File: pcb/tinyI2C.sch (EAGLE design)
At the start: 29 parts, among them IC1 74ABT125BQ, IC2 TPS73618(0.4A), U1 LPC824M201JHI33, X1 TSW-112-02-S-S, X2 TSW-106-02-S-S-RA, X3 TSW-112-02-S-S, X4 TSW-102-02-S-S, X5 TSW-102-02-S-S

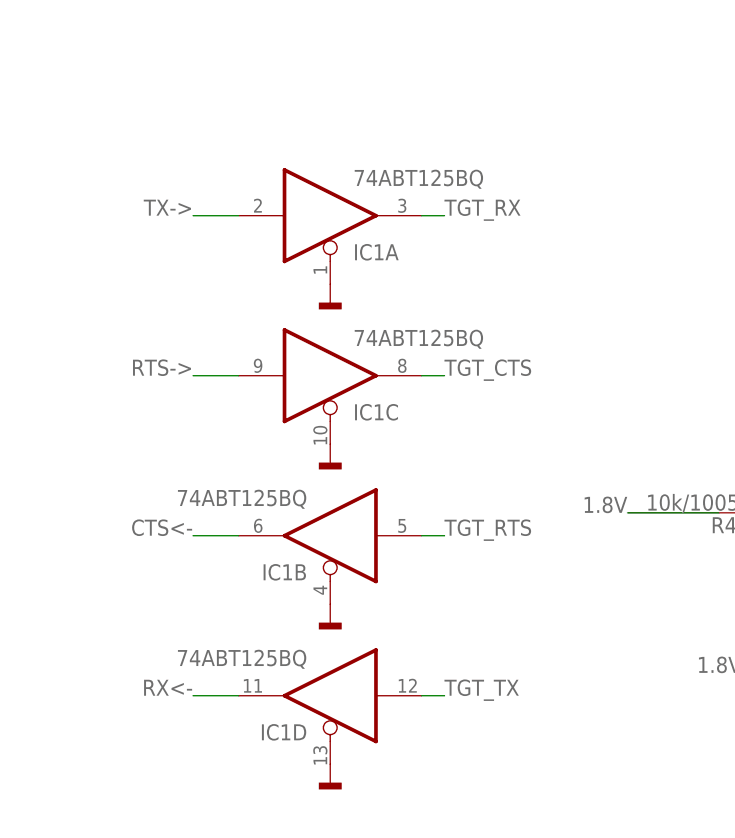
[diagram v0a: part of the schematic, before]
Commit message: [ PCB ][ SCH ][ BRD ] IC1, C5 update IC1: better footprint C5: smaller footprint
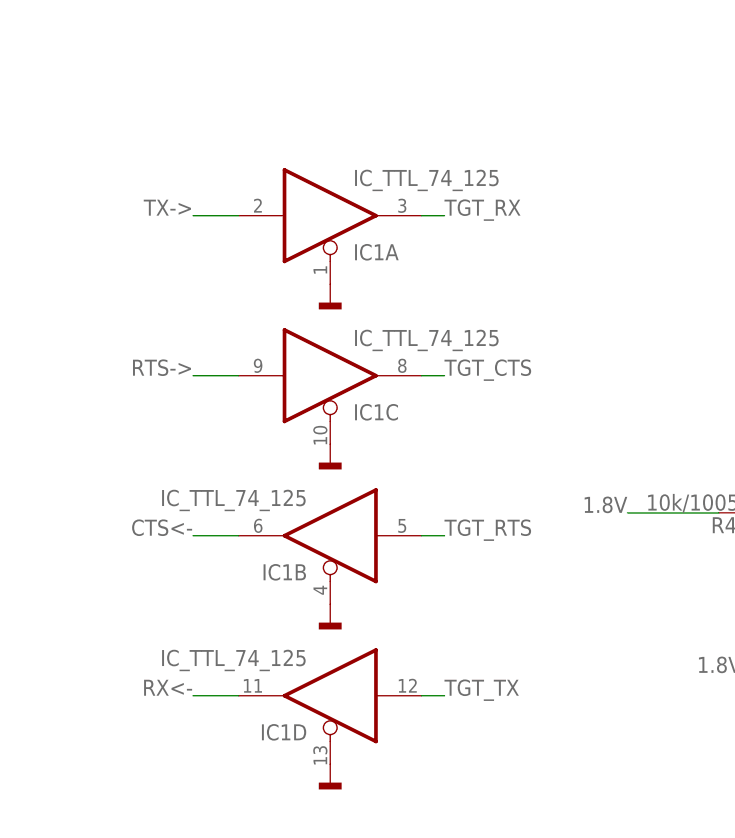
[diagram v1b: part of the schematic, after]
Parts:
- C5: device rcl:C-EUC1608 -> rcl:C-EUC0402
- IC1: value 74ABT125BQ -> IC_TTL_74_125; device 74xx-eu_local:74ABT125BQ -> mylib:IC_TTL_74_125
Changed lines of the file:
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@@
 <part name="C2" library="rcl" deviceset="C-EU" device="C1005" value="1005"/>
 <part name="C4" library="rcl" deviceset="C-EU" device="C1005" value="1005"/>
-<part name="C5" library="rcl" deviceset="C-EU" device="C1608" value="1608"/>
+<part name="C5" library="rcl" deviceset="C-EU" device="C0402" value="1608"/>
 <part name="GND9" library="mbed-HDK" deviceset="GND" device=""/>
 <part name="GND10" library="mbed-HDK" deviceset="GND" device=""/>
@@
 <part name="GND13" library="mbed-HDK" deviceset="GND" device=""/>
 <part name="C6" library="rcl" deviceset="C-EU" device="C1005" value="1005"/>
-<part name="IC1" library="74xx-eu_local" deviceset="74*125" device="BQ" technology="ABT"/>
+<part name="IC1" library="mylib" deviceset="IC_TTL_74_125" device=""/>
 <part name="X4" library="con-samtec.local" deviceset="TSW-102-02-S-S" device=""/>
 <part name="GND12" library="mbed-HDK" deviceset="GND" device=""/>

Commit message: [ PCB ][ SCH ] new header for ISP
added ISP header
removed connection to X1[3]
renamed other headers
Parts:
- added X6: TSW-102-02-S-S, con-samtec.local:TSW-102-02-S-S
- X2: value TSW-106-02-S-S-RA -> TSW-112-02-S-S; device con-samtec.local:TSW-106-02-S-S-RA -> con-samtec.local:TSW-112-02-S-S
- X3: value TSW-112-02-S-S -> TSW-106-02-S-S-RA; device con-samtec.local:TSW-112-02-S-S -> con-samtec.local:TSW-106-02-S-S-RA
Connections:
- net !ISP!: now also X6-1.1; no longer X1-3.1
- net 5V: now also X3-3.1; no longer X2-3.1
- net CTS<-: now also X3-2.1; no longer X2-2.1
- net GND: now also X3-1.1, X6-2.1; no longer X2-1.1
- net GPIO00: now also X2-1.1; no longer X3-1.1
- net GPIO01: now also X2-2.1; no longer X3-2.1
- net GPIO02: now also X2-3.1; no longer X3-3.1
- net GPIO03: now also X2-4.1; no longer X3-4.1
- net GPIO04: now also X2-5.1; no longer X3-5.1
- net GPIO05: now also X2-6.1; no longer X3-6.1
- net GPIO06: now also X2-7.1; no longer X3-7.1
- net GPIO07: now also X2-8.1; no longer X3-8.1
- net RTS->: now also X3-6.1; no longer X2-6.1
- net RX<-: now also X3-5.1; no longer X2-5.1
- net SPI_CS: now also X2-12.1; no longer X3-12.1
- net SPI_MISO: now also X2-10.1; no longer X3-10.1
- net SPI_MOSI: now also X2-9.1; no longer X3-9.1
- net SPI_SCK: now also X2-11.1; no longer X3-11.1
- net TX->: now also X3-4.1; no longer X2-4.1
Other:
- moved on the sheet: X2-1, X2-2, X2-3, X2-4, X2-5, X2-6, X3-1, X3-2, X3-3, X3-4, X3-5, X3-6
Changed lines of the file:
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@@
 <parts>
 <part name="FRAME1" library="frames" deviceset="A4L-LOC" device=""/>
-<part name="X2" library="con-samtec.local" deviceset="TSW-106-02-S-S" device="-RA"/>
+<part name="X3" library="con-samtec.local" deviceset="TSW-106-02-S-S" device="-RA"/>
 <part name="U1" library="mylib" deviceset="LPC824M201JHI33" device=""/>
 <part name="GND2" library="mbed-HDK" deviceset="GND" device=""/>
@@
 <part name="GND1" library="mbed-HDK" deviceset="GND" device=""/>
 <part name="X1" library="con-samtec.local" deviceset="TSW-112-02-S-S" device=""/>
-<part name="X3" library="con-samtec.local" deviceset="TSW-112-02-S-S" device=""/>
+<part name="X2" library="con-samtec.local" deviceset="TSW-112-02-S-S" device=""/>
 <part name="GND13" library="mbed-HDK" deviceset="GND" device=""/>
 <part name="C6" library="rcl" deviceset="C-EU" device="C1005" value="1005"/>
@@
 <part name="TP5" library="testpad" deviceset="TP" device="TP10R" value="TPTP10R"/>
 <part name="X5" library="con-samtec.local" deviceset="TSW-102-02-S-S" device=""/>
+<part name="X6" library="con-samtec.local" deviceset="TSW-102-02-S-S" device=""/>
+<part name="GND14" library="mbed-HDK" deviceset="GND" device=""/>
 </parts>
 <sheets>
@@
 <instances>
 <instance part="FRAME1" gate="G$1" x="0" y="0"/>
-<instance part="X2" gate="-1" x="30.48" y="40.64" smashed="yes" rot="R180">
+<instance part="X3" gate="-1" x="30.48" y="40.64" smashed="yes" rot="R180">
 <attribute name="VALUE" x="31.75" y="44.45" size="1.778" layer="96" rot="R180"/>
 <attribute name="NAME" x="27.94" y="41.402" size="1.524" layer="95" rot="R180"/>
 </instance>
-<instance part="X2" gate="-2" x="30.48" y="38.1" rot="R180"/>
-<instance part="X2" gate="-3" x="30.48" y="35.56" rot="R180"/>
-<instance part="X2" gate="-4" x="30.48" y="33.02" rot="R180"/>
-<instance part="X2" gate="-5" x="30.48" y="30.48" rot="R180"/>
-<instance part="X2" gate="-6" x="30.48" y="27.94" rot="R180"/>
+<instance part="X3" gate="-2" x="30.48" y="38.1" rot="R180"/>
+<instance part="X3" gate="-3" x="30.48" y="35.56" rot="R180"/>
+<instance part="X3" gate="-4" x="30.48" y="33.02" rot="R180"/>
+<instance part="X3" gate="-5" x="30.48" y="30.48" rot="R180"/>
+<instance part="X3" gate="-6" x="30.48" y="27.94" rot="R180"/>
 <instance part="U1" gate="G$1" x="106.68" y="121.92"/>
 <instance part="GND2" gate="1" x="35.56" y="88.9"/>
@@
 <instance part="X1" gate="-11" x="71.12" y="15.24"/>
 <instance part="X1" gate="-12" x="71.12" y="12.7"/>
-<instance part="X3" gate="-1" x="106.68" y="40.64"/>
-<instance part="X3" gate="-2" x="106.68" y="38.1"/>
-<instance part="X3" gate="-3" x="106.68" y="35.56"/>
-<instance part="X3" gate="-4" x="106.68" y="33.02"/>
-<instance part="X3" gate="-5" x="106.68" y="30.48"/>
-<instance part="X3" gate="-6" x="106.68" y="27.94"/>
-<instance part="X3" gate="-7" x="106.68" y="25.4"/>
-<instance part="X3" gate="-8" x="106.68" y="22.86"/>
-<instance part="X3" gate="-9" x="106.68" y="20.32"/>
-<instance part="X3" gate="-10" x="106.68" y="17.78"/>
-<instance part="X3" gate="-11" x="106.68" y="15.24"/>
-<instance part="X3" gate="-12" x="106.68" y="12.7"/>
+<instance part="X2" gate="-1" x="106.68" y="40.64"/>
+<instance part="X2" gate="-2" x="106.68" y="38.1"/>
+<instance part="X2" gate="-3" x="106.68" y="35.56"/>
+<instance part="X2" gate="-4" x="106.68" y="33.02"/>
+<instance part="X2" gate="-5" x="106.68" y="30.48"/>
+<instance part="X2" gate="-6" x="106.68" y="27.94"/>
+<instance part="X2" gate="-7" x="106.68" y="25.4"/>
+<instance part="X2" gate="-8" x="106.68" y="22.86"/>
+<instance part="X2" gate="-9" x="106.68" y="20.32"/>
+<instance part="X2" gate="-10" x="106.68" y="17.78"/>
+<instance part="X2" gate="-11" x="106.68" y="15.24"/>
+<instance part="X2" gate="-12" x="106.68" y="12.7"/>
 <instance part="GND13" gate="1" x="68.58" y="38.1" rot="R270"/>
 <instance part="C6" gate="G$1" x="165.1" y="88.9"/>
@@
 <instance part="X4" gate="-1" x="30.48" y="17.78" rot="MR0"/>
 <instance part="X4" gate="-2" x="30.48" y="15.748" rot="MR0"/>
-<instance part="GND12" gate="1" x="33.02" y="15.748"/>
+<instance part="GND12" gate="1" x="35.56" y="15.748"/>
 <instance part="TP4" gate="G$1" x="238.76" y="48.26" smashed="yes" rot="R90">
 <attribute name="NAME" x="238.252" y="47.244" size="1.778" layer="95" rot="MR0"/>
@@
 <instance part="X5" gate="-1" x="30.48" y="50.8" rot="MR0"/>
 <instance part="X5" gate="-2" x="30.48" y="48.26" rot="MR0"/>
+<instance part="X6" gate="-1" x="30.48" y="60.96" rot="MR0"/>
+<instance part="X6" gate="-2" x="30.48" y="58.42" rot="MR0"/>
+<instance part="GND14" gate="1" x="35.56" y="58.42"/>
 </instances>
 <busses>
@@
 <net name="CTS&lt;-" class="0">
 <segment>
-<pinref part="X2" gate="-2" pin="1"/>
+<pinref part="X3" gate="-2" pin="1"/>
 <wire x1="33.02" y1="38.1" x2="38.1" y2="38.1" width="0.1524" layer="91"/>
 <label x="38.1" y="38.1" size="1.778" layer="95"/>
@@
 <net name="5V" class="0">
 <segment>
-<pinref part="X2" gate="-3" pin="1"/>
+<pinref part="X3" gate="-3" pin="1"/>
 <label x="38.1" y="35.56" size="1.778" layer="95"/>
 <wire x1="33.02" y1="35.56" x2="38.1" y2="35.56" width="0.1524" layer="91"/>
@@
 <net name="TX-&gt;" class="0">
 <segment>
-<pinref part="X2" gate="-4" pin="1"/>
+<pinref part="X3" gate="-4" pin="1"/>
 <wire x1="33.02" y1="33.02" x2="38.1" y2="33.02" width="0.1524" layer="91"/>
 <label x="38.1" y="33.02" size="1.778" layer="95"/>
@@
 <net name="RX&lt;-" class="0">
 <segment>
-<pinref part="X2" gate="-5" pin="1"/>
+<pinref part="X3" gate="-5" pin="1"/>
 <wire x1="33.02" y1="30.48" x2="38.1" y2="30.48" width="0.1524" layer="91"/>
 <label x="38.1" y="30.48" size="1.778" layer="95"/>
@@
 <net name="RTS-&gt;" class="0">
 <segment>
-<pinref part="X2" gate="-6" pin="1"/>
+<pinref part="X3" gate="-6" pin="1"/>
 <wire x1="33.02" y1="27.94" x2="38.1" y2="27.94" width="0.1524" layer="91"/>
 <label x="38.1" y="27.94" size="1.778" layer="95"/>
@@
 </segment>
 <segment>
-<pinref part="X2" gate="-1" pin="1"/>
+<pinref part="X3" gate="-1" pin="1"/>
 <wire x1="33.02" y1="40.64" x2="38.1" y2="40.64" width="0.1524" layer="91"/>
 <label x="38.1" y="40.64" size="1.778" layer="95"/>
@@
 <pinref part="X4" gate="-2" pin="1"/>
 <pinref part="GND12" gate="1" pin="GND"/>
+<wire x1="35.56" y1="15.748" x2="33.02" y2="15.748" width="0.1524" layer="91"/>
+</segment>
+<segment>
+<pinref part="X6" gate="-2" pin="1"/>
+<pinref part="GND14" gate="1" pin="GND"/>
+<wire x1="33.02" y1="58.42" x2="35.56" y2="58.42" width="0.1524" layer="91"/>
 </segment>
 </net>
@@
 </segment>
 <segment>
-<wire x1="63.5" y1="35.56" x2="68.58" y2="35.56" width="0.1524" layer="91"/>
-<pinref part="X1" gate="-3" pin="1"/>
-<label x="63.5" y="35.56" size="1.778" layer="95" rot="MR0"/>
+<wire x1="33.02" y1="60.96" x2="38.1" y2="60.96" width="0.1524" layer="91"/>
+<pinref part="X6" gate="-1" pin="1"/>
+<label x="38.1" y="60.96" size="1.778" layer="95"/>
 </segment>
 </net>
@@
 <segment>
 <wire x1="99.06" y1="15.24" x2="104.14" y2="15.24" width="0.1524" layer="91"/>
-<pinref part="X3" gate="-11" pin="1"/>
+<pinref part="X2" gate="-11" pin="1"/>
 <label x="99.06" y="15.24" size="1.778" layer="95" rot="MR0"/>
 </segment>
@@
 <segment>
 <wire x1="99.06" y1="12.7" x2="104.14" y2="12.7" width="0.1524" layer="91"/>
-<pinref part="X3" gate="-12" pin="1"/>
+<pinref part="X2" gate="-12" pin="1"/>
 <label x="99.06" y="12.7" size="1.778" layer="95" rot="MR0"/>
 </segment>
@@
 <segment>
 <wire x1="104.14" y1="17.78" x2="99.06" y2="17.78" width="0.1524" layer="91"/>
-<pinref part="X3" gate="-10" pin="1"/>
+<pinref part="X2" gate="-10" pin="1"/>
 <label x="99.06" y="17.78" size="1.778" layer="95" rot="MR0"/>
 </segment>
@@
 <segment>
 <wire x1="99.06" y1="20.32" x2="104.14" y2="20.32" width="0.1524" layer="91"/>
-<pinref part="X3" gate="-9" pin="1"/>
+<pinref part="X2" gate="-9" pin="1"/>
 <label x="99.06" y="20.32" size="1.778" layer="95" rot="MR0"/>
 </segment>
@@
 <wire x1="99.06" y1="22.86" x2="104.14" y2="22.86" width="0.1524" layer="91"/>
 <label x="99.06" y="22.86" size="1.778" layer="95" rot="MR0"/>
-<pinref part="X3" gate="-8" pin="1"/>
+<pinref part="X2" gate="-8" pin="1"/>
 </segment>
 </net>
@@
 <wire x1="104.14" y1="25.4" x2="99.06" y2="25.4" width="0.1524" layer="91"/>
 <label x="99.06" y="25.4" size="1.778" layer="95" rot="MR0"/>
-<pinref part="X3" gate="-7" pin="1"/>
+<pinref part="X2" gate="-7" pin="1"/>
 </segment>
 </net>
@@
 <wire x1="99.06" y1="27.94" x2="104.14" y2="27.94" width="0.1524" layer="91"/>
 <label x="99.06" y="27.94" size="1.778" layer="95" rot="MR0"/>
-<pinref part="X3" gate="-6" pin="1"/>
+<pinref part="X2" gate="-6" pin="1"/>
 </segment>
 </net>
@@
 <wire x1="104.14" y1="30.48" x2="99.06" y2="30.48" width="0.1524" layer="91"/>
 <label x="99.06" y="30.48" size="1.778" layer="95" rot="MR0"/>
-<pinref part="X3" gate="-5" pin="1"/>
+<pinref part="X2" gate="-5" pin="1"/>
 </segment>
 </net>
@@
 <wire x1="99.06" y1="33.02" x2="104.14" y2="33.02" width="0.1524" layer="91"/>
 <label x="99.06" y="33.02" size="1.778" layer="95" rot="MR0"/>
-<pinref part="X3" gate="-4" pin="1"/>
+<pinref part="X2" gate="-4" pin="1"/>
 </segment>
 </net>
@@
 <segment>
 <wire x1="104.14" y1="35.56" x2="99.06" y2="35.56" width="0.1524" layer="91"/>
-<pinref part="X3" gate="-3" pin="1"/>
+<pinref part="X2" gate="-3" pin="1"/>
 <label x="99.06" y="35.56" size="1.778" layer="95" rot="MR0"/>
 </segment>
@@
 <segment>
 <wire x1="99.06" y1="38.1" x2="104.14" y2="38.1" width="0.1524" layer="91"/>
-<pinref part="X3" gate="-2" pin="1"/>
+<pinref part="X2" gate="-2" pin="1"/>
 <label x="99.06" y="38.1" size="1.778" layer="95" rot="MR0"/>
 </segment>
@@
 <segment>
 <wire x1="104.14" y1="40.64" x2="99.06" y2="40.64" width="0.1524" layer="91"/>
-<pinref part="X3" gate="-1" pin="1"/>
+<pinref part="X2" gate="-1" pin="1"/>
 <label x="99.06" y="40.64" size="1.778" layer="95" rot="MR0"/>
 </segment>

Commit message: [ PCB ][ SCH ] LDO and buffer replace
LDO replaced to MIC5355(Micron, 2 outputs) IC2-> IC3
(Vout1 = 3.3V, Vout2 = 1.8V)
125 buffer replaced to 2x single chip buffers(IC1,IC2) package: SC-70
3.3V line added
C7 added for 3.3V buffer
C3 changed for 3.3V line
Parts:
- added C7: 1005, rcl:C-EUC1005
- added IC3: IC_LDO_MIC5355, mylib:IC_LDO_MIC5355
- added TP6: TPTP07R, testpad:TPTP07R
- IC1: value IC_TTL_74_125 -> 74LVC1G125DCK; device mylib:IC_TTL_74_125 -> 74xx-little-us:74LVC1G125DCK
- IC2: value TPS73618(0.4A) -> 74LVC1G125DCK; device mylib:TPS73618DBVT -> 74xx-little-us:74LVC1G125DCK
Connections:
- removed net CTS<-: IC1B.O, X3-2.1
- removed net N$1: C3.1, IC2.NC/FB
- removed net RTS->: IC1C.I, X3-6.1
- removed net TGT_CTS: IC1C.O, U1.P0_1
- removed net TGT_RTS: IC1B.I, U1.P0_13
- new net 3.3V: C3.1, C7.1, IC1P.VCC, IC3.VOUT1, TP6.TP
- net 1.8V: now also IC2P.VCC, IC3.VOUT2; no longer IC1P.VCC, IC2.OUT
- net 5V: now also IC3.EN1, IC3.EN2, IC3.VIN; no longer IC2.!EN, IC2.IN
- net GND: now also C7.2, IC2A.OE, IC2P.GND, IC3.GND; no longer IC1B.OE, IC1C.OE, IC1D.OE, IC2.GND
- net RX<-: now also IC1A.O; no longer IC1D.O
- net TGT_RX: now also IC2A.O; no longer IC1A.O
- net TGT_TX: now also IC1A.I; no longer IC1D.I
- net TX->: now also IC2A.I; no longer IC1A.I
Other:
- moved on the sheet: C1, C3, IC1, IC1P

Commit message: [ PCB ][ BED ] new header X7 addition related move added silk for ISP/RST font size change: 1.0,1.2,1.3mm/15%
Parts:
- added X7: TSW-102-02-S-S, con-samtec.local:TSW-102-02-S-S
- IC1, IC2: device 74xx-little-us:74LVC1G125DCK -> 74xx-little-us_local:74LVC1G125DCK
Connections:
- new net P0_1: U1.P0_1, X7-2.1
- new net P0_13: U1.P0_13, X7-1.1
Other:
- moved on the sheet: C1, C7, IC1P, IC2P
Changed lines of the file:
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@@
 <part name="GND15" library="mbed-HDK" deviceset="GND" device=""/>
 <part name="TP6" library="testpad" deviceset="TP" device="TP07R"/>
-<part name="IC1" library="74xx-little-us" deviceset="74*1G125" device="DCK" technology="LVC"/>
-<part name="IC2" library="74xx-little-us" deviceset="74*1G125" device="DCK" technology="LVC"/>
+<part name="IC1" library="74xx-little-us_local" deviceset="74*1G125" device="DCK" technology="LVC"/>
+<part name="IC2" library="74xx-little-us_local" deviceset="74*1G125" device="DCK" technology="LVC"/>
 <part name="C7" library="rcl" deviceset="C-EU" device="C1005" value="1005"/>
 <part name="IC3" library="mylib" deviceset="IC_LDO_MIC5355" device=""/>
+<part name="X7" library="con-samtec.local" deviceset="TSW-102-02-S-S" device=""/>
 </parts>
 <sheets>
@@
 <instance part="GND7" gate="1" x="182.88" y="111.76"/>
 <instance part="GND8" gate="1" x="210.82" y="76.2"/>
-<instance part="C1" gate="G$1" x="68.58" y="68.58"/>
+<instance part="C1" gate="G$1" x="45.72" y="96.52"/>
 <instance part="C2" gate="G$1" x="170.18" y="88.9"/>
 <instance part="C4" gate="G$1" x="243.84" y="83.82"/>
 <instance part="C5" gate="G$1" x="205.74" y="83.82"/>
-<instance part="GND9" gate="1" x="68.58" y="60.96"/>
+<instance part="GND9" gate="1" x="45.72" y="88.9"/>
 <instance part="GND10" gate="1" x="243.84" y="76.2"/>
 <instance part="GND11" gate="1" x="170.18" y="81.28"/>
@@
 <instance part="IC1" gate="A" x="35.56" y="124.46" rot="R180"/>
 <instance part="IC2" gate="A" x="35.56" y="149.86" rot="MR180"/>
-<instance part="IC2" gate="P" x="60.96" y="68.58"/>
-<instance part="IC1" gate="P" x="45.72" y="68.58"/>
-<instance part="C7" gate="G$1" x="53.34" y="71.12"/>
+<instance part="IC2" gate="P" x="38.1" y="96.52"/>
+<instance part="IC1" gate="P" x="22.86" y="96.52"/>
+<instance part="C7" gate="G$1" x="30.48" y="99.06"/>
 <instance part="IC3" gate="G$1" x="208.28" y="111.76"/>
+<instance part="X7" gate="-1" x="30.48" y="71.12" rot="MR0"/>
+<instance part="X7" gate="-2" x="30.48" y="68.58" rot="MR0"/>
 </instances>
 <busses>
@@
 <pinref part="C1" gate="G$1" pin="2"/>
 <pinref part="GND9" gate="1" pin="GND"/>
-<wire x1="68.58" y1="63.5" x2="68.58" y2="60.96" width="0.1524" layer="91"/>
-<wire x1="68.58" y1="60.96" x2="60.96" y2="60.96" width="0.1524" layer="91"/>
-<junction x="68.58" y="60.96"/>
+<wire x1="45.72" y1="91.44" x2="45.72" y2="88.9" width="0.1524" layer="91"/>
+<wire x1="45.72" y1="88.9" x2="38.1" y2="88.9" width="0.1524" layer="91"/>
+<junction x="45.72" y="88.9"/>
 <pinref part="IC2" gate="P" pin="GND"/>
 <pinref part="IC1" gate="P" pin="GND"/>
-<wire x1="45.72" y1="60.96" x2="53.34" y2="60.96" width="0.1524" layer="91"/>
-<junction x="60.96" y="60.96"/>
+<wire x1="22.86" y1="88.9" x2="30.48" y2="88.9" width="0.1524" layer="91"/>
+<junction x="38.1" y="88.9"/>
 <pinref part="C7" gate="G$1" pin="2"/>
-<wire x1="53.34" y1="60.96" x2="60.96" y2="60.96" width="0.1524" layer="91"/>
-<wire x1="53.34" y1="66.04" x2="53.34" y2="60.96" width="0.1524" layer="91"/>
-<junction x="53.34" y="60.96"/>
+<wire x1="30.48" y1="88.9" x2="38.1" y2="88.9" width="0.1524" layer="91"/>
+<wire x1="30.48" y1="93.98" x2="30.48" y2="88.9" width="0.1524" layer="91"/>
+<junction x="30.48" y="88.9"/>
 </segment>
 <segment>
@@
 </segment>
 <segment>
-<label x="71.12" y="76.2" size="1.778" layer="95"/>
-<wire x1="68.58" y1="76.2" x2="71.12" y2="76.2" width="0.1524" layer="91"/>
+<label x="48.26" y="104.14" size="1.778" layer="95"/>
+<wire x1="45.72" y1="104.14" x2="48.26" y2="104.14" width="0.1524" layer="91"/>
 <pinref part="C1" gate="G$1" pin="1"/>
-<wire x1="68.58" y1="71.12" x2="68.58" y2="76.2" width="0.1524" layer="91"/>
+<wire x1="45.72" y1="99.06" x2="45.72" y2="104.14" width="0.1524" layer="91"/>
 <pinref part="IC2" gate="P" pin="VCC"/>
-<wire x1="60.96" y1="76.2" x2="68.58" y2="76.2" width="0.1524" layer="91"/>
-<junction x="68.58" y="76.2"/>
+<wire x1="38.1" y1="104.14" x2="45.72" y2="104.14" width="0.1524" layer="91"/>
+<junction x="45.72" y="104.14"/>
 </segment>
 <segment>
@@
 <segment>
 <pinref part="C7" gate="G$1" pin="1"/>
-<wire x1="53.34" y1="73.66" x2="53.34" y2="76.2" width="0.1524" layer="91"/>
+<wire x1="30.48" y1="101.6" x2="30.48" y2="104.14" width="0.1524" layer="91"/>
 <pinref part="IC1" gate="P" pin="VCC"/>
-<wire x1="53.34" y1="76.2" x2="45.72" y2="76.2" width="0.1524" layer="91"/>
-<wire x1="45.72" y1="76.2" x2="40.64" y2="76.2" width="0.1524" layer="91"/>
-<junction x="45.72" y="76.2"/>
-<label x="40.64" y="76.2" size="1.778" layer="95" rot="MR0"/>
-</segment>
-</net>
+<wire x1="30.48" y1="104.14" x2="22.86" y2="104.14" width="0.1524" layer="91"/>
+<wire x1="22.86" y1="104.14" x2="17.78" y2="104.14" width="0.1524" layer="91"/>
+<junction x="22.86" y="104.14"/>
+<label x="17.78" y="104.14" size="1.778" layer="95" rot="MR0"/>
+</segment>
+</net>
+<net name="P0_1" class="0">
+<segment>
+<pinref part="U1" gate="G$1" pin="P0_1"/>
+<wire x1="144.78" y1="83.82" x2="144.78" y2="78.74" width="0.1524" layer="91"/>
+<label x="144.78" y="78.74" size="1.778" layer="95" rot="MR270"/>
+</segment>
+<segment>
+<wire x1="33.02" y1="68.58" x2="38.1" y2="68.58" width="0.1524" layer="91"/>
+<label x="38.1" y="68.58" size="1.778" layer="95"/>
+<pinref part="X7" gate="-2" pin="1"/>
+</segment>
+</net>
+<net name="P0_13" class="0">
+<segment>
+<pinref part="U1" gate="G$1" pin="P0_13"/>
+<wire x1="106.68" y1="121.92" x2="101.6" y2="121.92" width="0.1524" layer="91"/>
+<label x="101.6" y="121.92" size="1.778" layer="95" rot="MR0"/>
+</segment>
+<segment>
+<wire x1="38.1" y1="71.12" x2="33.02" y2="71.12" width="0.1524" layer="91"/>
+<pinref part="X7" gate="-1" pin="1"/>
+<label x="38.1" y="71.12" size="1.778" layer="95"/>
+</segment>
+</net>
